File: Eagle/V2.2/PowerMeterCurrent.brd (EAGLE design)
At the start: 100 x 80 mm, 59 parts, among them IC1 4067D, IC2 4514D, X1 STEREOJACK, X10 STEREOJACK, X11 STEREOJACK, X12 STEREOJACK, X13 STEREOJACK, X14 STEREOJACK, X15 STEREOJACK, X16 STEREOJACK, X2 STEREOJACK, X3 STEREOJACK, X4 STEREOJACK, X5 STEREOJACK, X6 STEREOJACK, X7 STEREOJACK, X8 STEREOJACK, X9 STEREOJACK

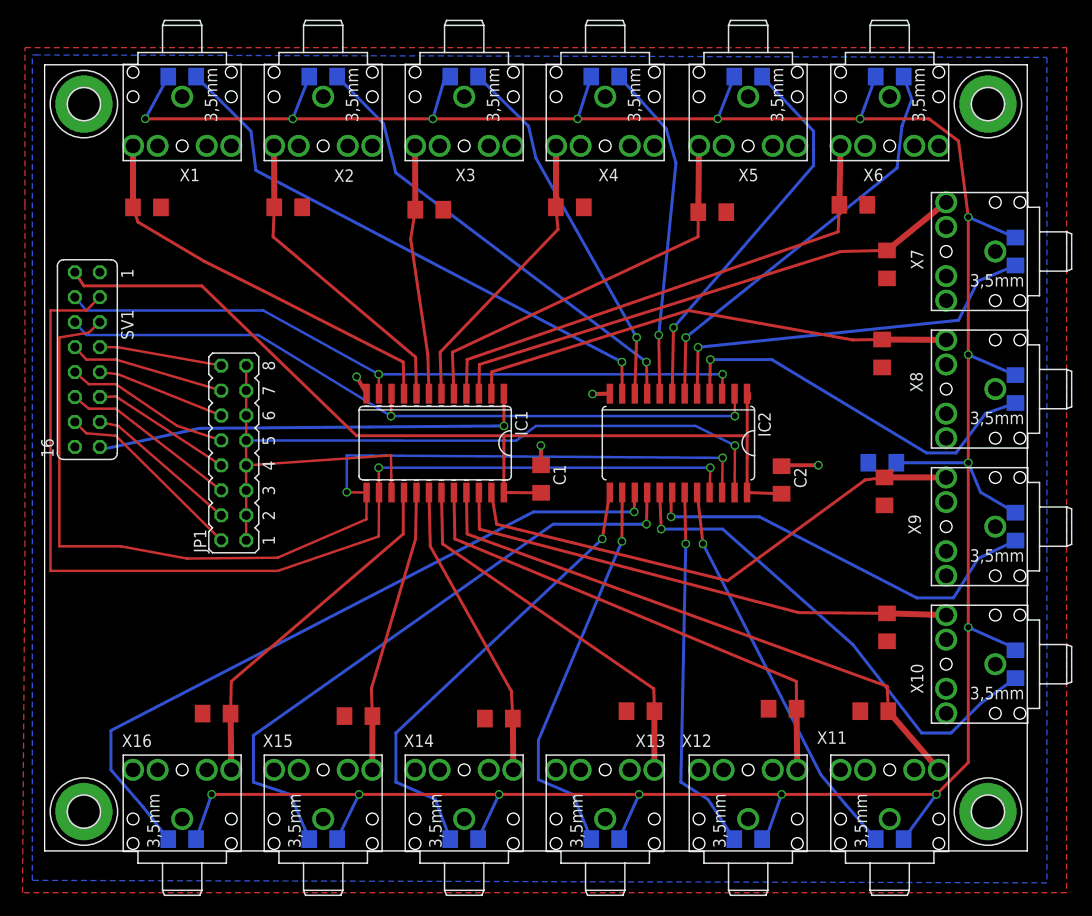
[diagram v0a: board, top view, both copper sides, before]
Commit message: Cleaned up some thing
cleaned up traces, made 3.5mm connectors, caps & diode SMD, put everything on same side of boards (may need to put resistor arrays back on the underside of the main board).
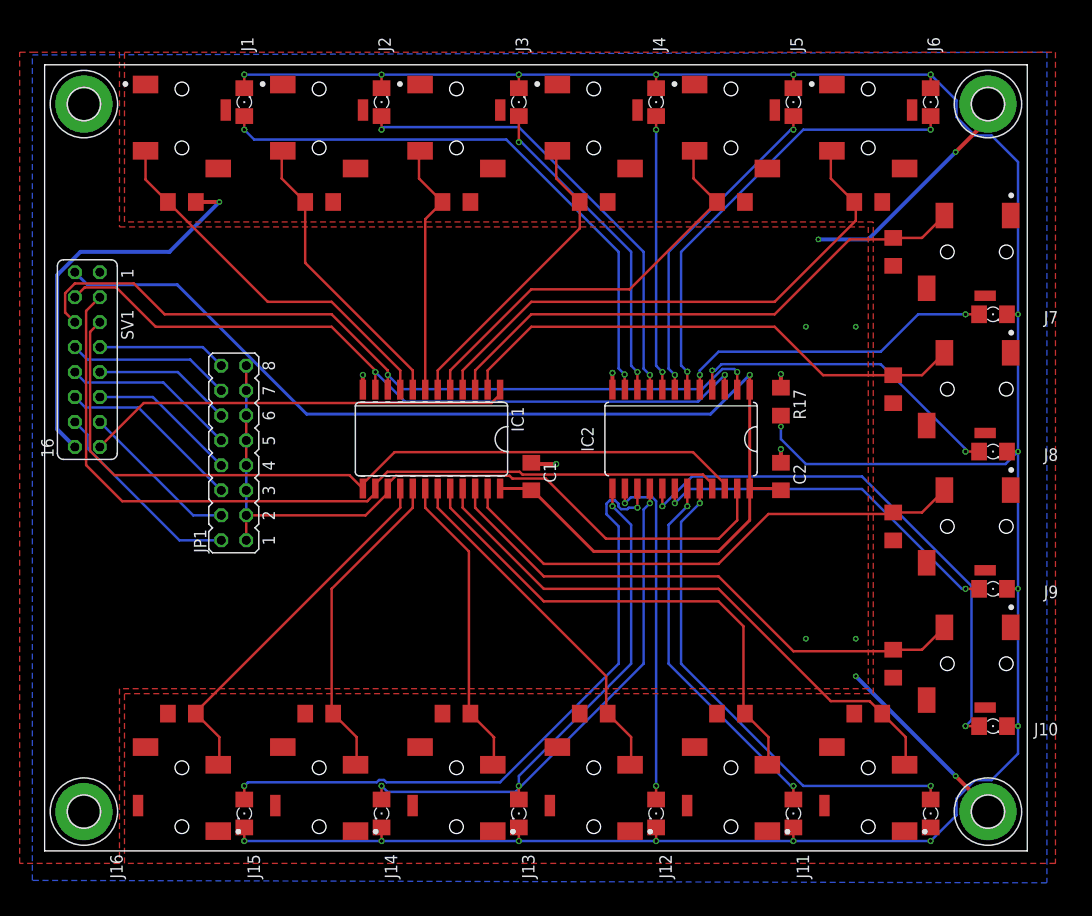
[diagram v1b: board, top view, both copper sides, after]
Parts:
- removed X1, X10, X11, X12, X13, X14, X15, X16, X2, X3, X4, X5, X6, X7, X8, X9: STEREOJACK, adafruit:STX3100
- added J1, J10, J11, J12, J13, J14, J15, J16, J2, J3, J4, J5, J6, J7, J8, J9: SJ2-35813B-SMT-TR, SJ2-35813B-SMT-TR:CUI_SJ2-35813B-SMT-TR
- moved R17 12.0 mm to (74.9, 45.7), flipped to the top, turned to 270 degrees
- moved LED16 6.84 mm to (20.3, 3.81), flipped to the top, turned to 270 degrees
- moved LED1 6.83 mm to (20.3, 76.2), flipped to the top, turned to 90 degrees
- moved LED7 6.78 mm to (96.5, 54.6), flipped to the top, turned to 0 degrees
- moved LED8 6.76 mm to (96.5, 40.6), flipped to the top, turned to 0 degrees
- moved LED9 6.73 mm to (96.5, 26.7), flipped to the top, turned to 0 degrees
- moved LED10 6.70 mm to (96.5, 12.7), flipped to the top, turned to 0 degrees
- moved LED15 6.49 mm to (34.3, 3.81), flipped to the top, turned to 270 degrees
- moved LED2 6.48 mm to (34.3, 76.2), flipped to the top, turned to 90 degrees
- moved LED14 6.14 mm to (48.3, 3.81), flipped to the top, turned to 270 degrees
- moved LED3 6.14 mm to (48.3, 76.2), flipped to the top, turned to 90 degrees
- moved LED13 5.80 mm to (62.2, 3.81), flipped to the top, turned to 270 degrees
- moved LED4 5.80 mm to (62.2, 76.2), flipped to the top, turned to 90 degrees
- moved LED12 5.29 mm to (76.2, 3.81), flipped to the top, turned to 270 degrees
- moved LED5 5.28 mm to (76.2, 76.2), flipped to the top, turned to 90 degrees
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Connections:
- removed net N$12: R1.2, R10.2, R11.2, R12.2, R13.2, R14.2, R15.2, R16.2, R2.2, R3.2, R4.2, R5.2, R6.2, R7.2, R8.2, R9.2, SV1.16, X1.1, X1.4, X10.1, X10.4, X11.1, X11.4, X12.1, X12.4, X13.1, X13.4, X14.1, X14.4, X15.1, X15.4, X16.1, X16.4, X2.1, X2.4, X3.1, X3.4, X4.1, X4.4, X5.1, X5.4, X6.1, X6.4, X7.1, X7.4, X8.1, X8.4, X9.1, X9.4
- new net CT-: J1.1, J1.10, J10.1, J10.10, J11.1, J11.10, J12.1, J12.10, J13.1, J13.10, J14.1, J14.10, J15.1, J15.10, J16.1, J16.10, J2.1, J2.10, J3.1, J3.10, J4.1, J4.10, J5.1, J5.10, J6.1, J6.10, J7.1, J7.10, J8.1, J8.10, J9.1, J9.10, R1.2, R10.2, R11.2, R12.2, R13.2, R14.2, R15.2, R16.2, R2.2, R3.2, R4.2, R5.2, R6.2, R7.2, R8.2, R9.2, SV1.16
- net N$18: now also J5.2; no longer X5.5
- net N$20: now also J1.2; no longer X1.5
- net N$22: now also J2.2; no longer X2.5
- net N$23: now also J3.2; no longer X3.5
- net N$24: now also J4.2; no longer X4.5
- net N$25: now also J6.2; no longer X6.5
- net N$26: now also J7.2; no longer X7.5
- net N$28: now also J8.2; no longer X8.5
- net N$29: now also J9.2; no longer X9.5
- net N$50: now also J10.2; no longer X10.5
- net N$51: now also J11.2; no longer X11.5
- net N$58: now also J12.2; no longer X12.5
- net N$59: now also J14.2; no longer X14.5
- net N$60: now also J15.2; no longer X15.5
- net N$66: now also J13.2; no longer X13.5
- net N$68: now also J16.2; no longer X16.5
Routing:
- net GND: track 9.56 -> 52.6 mm, vias 4 -> 13
- net CT-: track 0.00 -> 40.2 mm, vias 0 -> 1
- net N$21: track 314.5 -> 274.8 mm, vias 16 -> 17
- net VDD: track 99.0 -> 125.2 mm, vias 0 -> 1
- net N$5: track 108.3 -> 83.3 mm, vias 2 -> 0
- net N$4: track 109.3 -> 85.7 mm, vias 2 -> 0
- net N$6: track 92.1 -> 76.6 mm, vias 1 -> 0
- net N$9: track 63.7 -> 51.8 mm, vias 1 -> 2
- net N$34: track 40.2 -> 50.6 mm, vias 1 -> 2
- net N$19: track 47.3 -> 37.2 mm, vias 1 -> 2
- net N$42: track 40.0 -> 32.7 mm, vias 1 -> 2
- net N$1: track 74.6 -> 81.2 mm
- net N$2: track 73.8 -> 67.5 mm, vias 1 -> 2
- net N$48: track 34.3 -> 28.1 mm, vias 1 -> 2
- net N$40: track 39.3 -> 33.2 mm, vias 1 -> 2
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- added copper zone on layer 1, net CT-
- added copper zone on layer 1, net GND
- removed copper zone on layer 1, net N$12
